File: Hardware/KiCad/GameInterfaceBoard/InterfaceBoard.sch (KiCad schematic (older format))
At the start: 34 parts, among them J1 CONN_11LOCK, J2 CONN_07LOCK

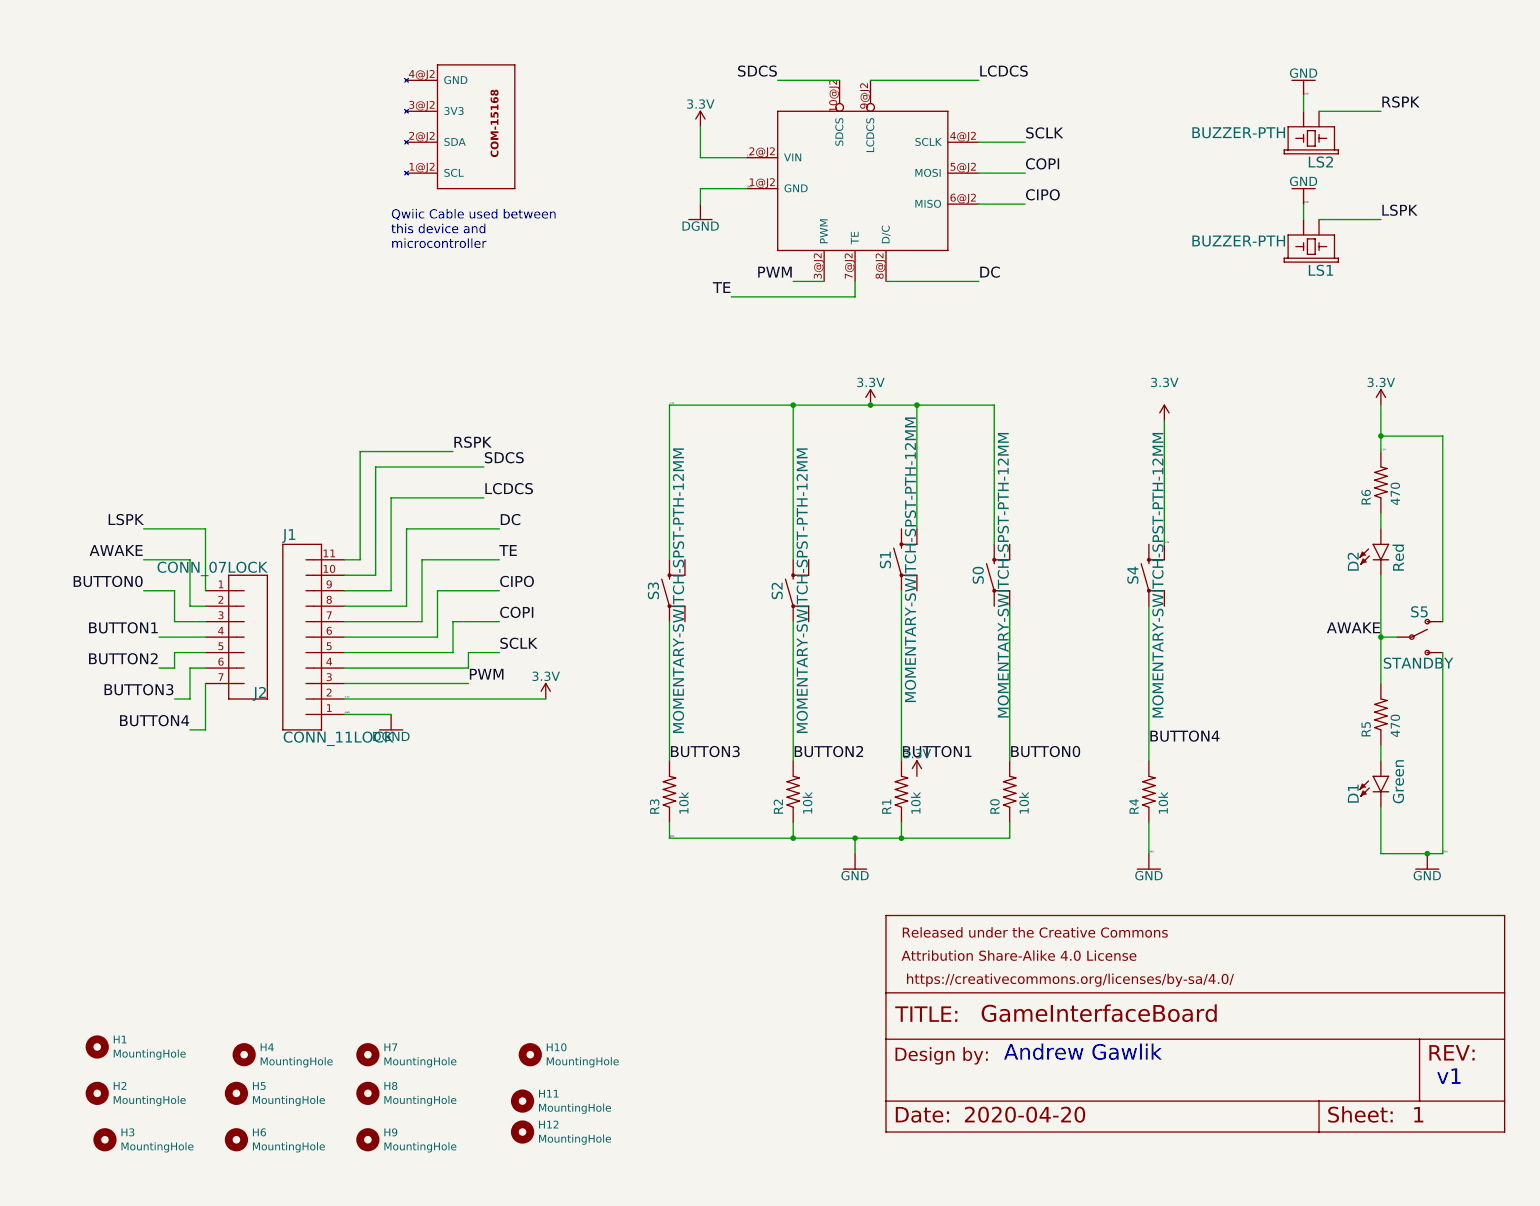
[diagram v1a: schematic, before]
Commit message: Removed excess drill holes as requested on issue #17
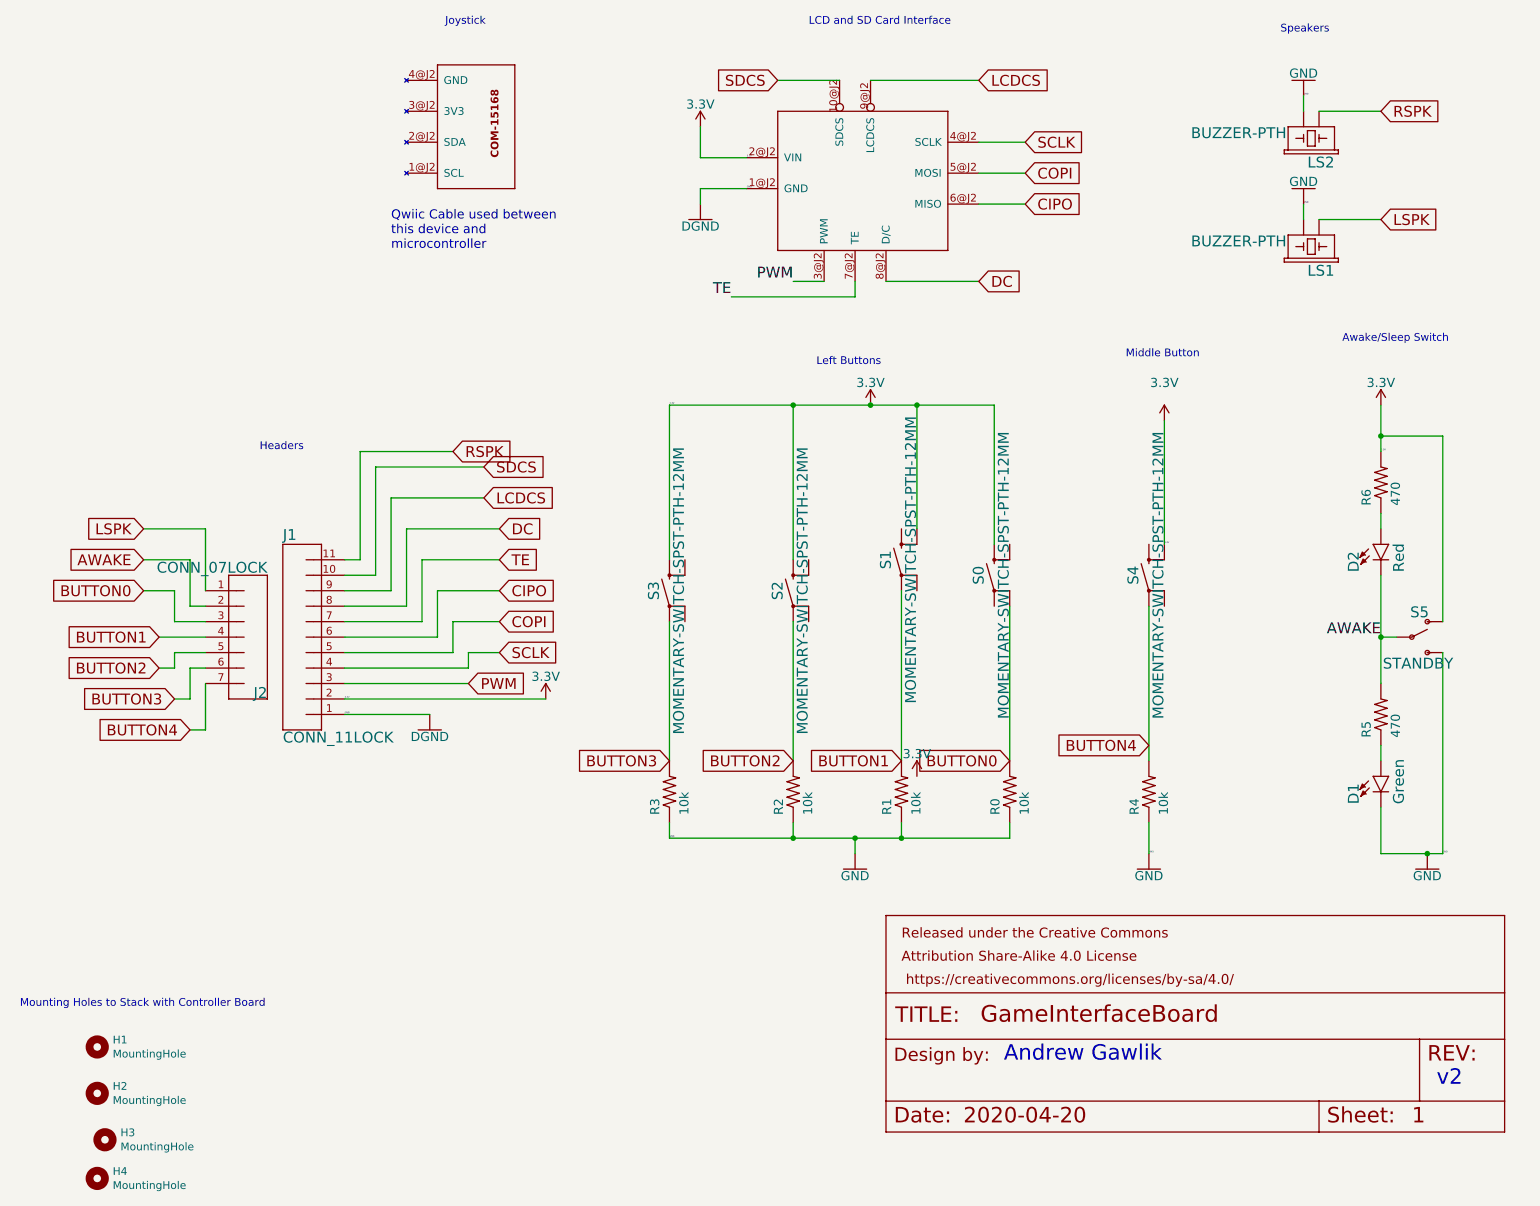
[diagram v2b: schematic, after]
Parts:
- removed H10, H11, H12, H5, H6, H7, H8, H9: MountingHole, MountingHole_3mm, symbol Mechanical:MountingHole
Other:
- note added: "Awake/Sleep Switch"
- note added: "Headers"
- note added: "Joystick"
- note added: "LCD and SD Card Interface"
- note added: "Left Buttons"
- note added: "Middle Button"
- note added: "Mounting Holes to Stack with Controller Board"
- note added: "Speakers"
- note added: "v2"
- note removed: "v1"
- moved on the sheet: H4
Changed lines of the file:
@@
 Wire Wire Line
 	5500 5600 5500 4700
-Text Label 5500 5600 0    70   ~ 0
-BUTTON3
 Wire Wire Line
 	2500 5000 2400 5000
@@
 Wire Wire Line
 	2400 5200 2300 5200
-Text Label 2300 5200 2    70   ~ 0
-BUTTON3
 Wire Wire Line
 	7700 4600 7700 5600
-Text Label 7700 5600 0    70   ~ 0
-BUTTON0
 Wire Wire Line
 	2500 4700 2300 4700
@@
 Wire Wire Line
 	2300 4500 2100 4500
-Text Label 2100 4500 2    70   ~ 0
-BUTTON0
 Wire Wire Line
 	6300 5600 6300 4700
-Text Label 6300 5600 0    70   ~ 0
-BUTTON2
 Wire Wire Line
 	2500 4900 2300 4900
@@
 Wire Wire Line
 	2300 5000 2200 5000
-Text Label 2200 5000 2    70   ~ 0
-BUTTON2
 Wire Wire Line
 	7000 4500 7000 5600
-Text Label 7000 5600 0    70   ~ 0
-BUTTON1
 Wire Wire Line
 	2500 4800 2200 4800
-Text Label 2200 4800 2    70   ~ 0
-BUTTON1
 Wire Wire Line
 	8600 6200 8600 6000
@@
 Text Label 6000 1900 0    10   ~ 0
 GND
-Wire Wire Line
-	3400 5300 3700 5300
 Text Label 3400 5300 0    10   ~ 0
 GND
@@
 Wire Wire Line
 	8600 4600 8600 5600
-Text Label 8600 5500 0    70   ~ 0
-BUTTON4
 Wire Wire Line
 	2500 5100 2500 5400
 Wire Wire Line
 	2500 5400 2400 5400
-Text Label 2400 5400 2    70   ~ 0
-BUTTON4
 Wire Wire Line
 	10100 5600 10100 5500
@@
 Wire Wire Line
 	2400 4300 2100 4300
-Text Label 2100 4300 2    70   ~ 0
-AWAKE
 Wire Wire Line
 	10100 4100 10100 4000
 Wire Wire Line
 	9700 2100 10100 2100
-Text Label 10100 2100 0    70   ~ 0
-LSPK
 Wire Wire Line
 	2500 4500 2500 4100
 Wire Wire Line
 	2500 4100 2100 4100
-Text Label 2100 4100 2    70   ~ 0
-LSPK
 Wire Wire Line
 	6500 2500 6300 2500
@@
 Wire Wire Line
 	3400 5100 4200 5100
-Text Label 4200 5100 0    70   ~ 0
-PWM
 Wire Wire Line
 	6700 2500 6700 2600
@@
 Wire Wire Line
 	3900 4300 4400 4300
-Text Label 4400 4300 0    70   ~ 0
-TE
 Wire Wire Line
 	6900 2500 7500 2500
-Text Label 7500 2500 0    70   ~ 0
-DC
 Wire Wire Line
 	3400 4600 3800 4600
@@
 Wire Wire Line
 	3800 4100 4400 4100
-Text Label 4400 4100 0    70   ~ 0
-DC
 Wire Wire Line
 	7500 2000 7800 2000
-Text Label 7800 2000 0    70   ~ 0
-CIPO
 Wire Wire Line
 	4000 4500 4400 4500
@@
 Wire Wire Line
 	4000 4800 4000 4500
-Text Label 4400 4500 0    70   ~ 0
-CIPO
 Wire Wire Line
 	7500 1800 7800 1800
-Text Label 7800 1800 0    70   ~ 0
-COPI
 Wire Wire Line
 	3400 4900 4100 4900
@@
 Wire Wire Line
 	4100 4700 4400 4700
-Text Label 4400 4700 0    70   ~ 0
-COPI
 Wire Wire Line
 	7500 1600 7800 1600
-Text Label 7800 1600 0    70   ~ 0
-SCLK
 Wire Wire Line
 	3400 5000 4200 5000
@@
 Wire Wire Line
 	4200 4900 4400 4900
-Text Label 4400 4900 0    70   ~ 0
-SCLK
 Wire Wire Line
 	6800 1200 7500 1200
-Text Label 7500 1200 0    70   ~ 0
-LCDCS
 Wire Wire Line
 	3400 4500 3700 4500
@@
 Wire Wire Line
 	3700 3900 4300 3900
-Text Label 4300 3900 0    70   ~ 0
-LCDCS
 Wire Wire Line
 	6600 1200 6200 1200
-Text Label 6200 1200 2    70   ~ 0
-SDCS
 Wire Wire Line
 	3400 4400 3600 4400
@@
 Wire Wire Line
 	3600 3700 4300 3700
-Text Label 4300 3700 0    70   ~ 0
-SDCS
 Wire Wire Line
 	9700 1400 10100 1400
-Text Label 10100 1400 0    70   ~ 0
-RSPK
 Wire Wire Line
 	3400 4300 3500 4300
@@
 Wire Wire Line
 	3500 3600 4100 3600
-Text Label 4100 3600 0    70   ~ 0
-RSPK
 $Comp
 L InterfaceBoard-eagle-import:R-US_0204_5 R2
@@
 $EndComp
 $Comp
-L InterfaceBoard-eagle-import:DGND #GND02
-U 1 1 13A376EC
-P 3700 5400
-F 0 "#GND02" H 3700 5400 50  0001 C CNN
-F 1 "DGND" H 3700 5390 59  0000 C TNN
-F 2 "" H 3700 5400 50  0001 C CNN
-F 3 "" H 3700 5400 50  0001 C CNN
-	1    3700 5400
-	1    0    0    -1
-$EndComp
-$Comp
 L InterfaceBoard-eagle-import:CONN_11LOCK J1
 U 1 1 2CE6A523
@@
 Andrew Gawlik
 Text Notes 10460 7710 0    100  ~ 0
-v1
+v2
 Text Notes 3700 2300 0    59   ~ 0
 Qwiic Cable used between\nthis device and\nmicrocontroller
@@
 L Mechanical:MountingHole H4
 U 1 1 60808813
-P 2750 7500
-F 0 "H4" H 2850 7546 50  0000 L CNN
-F 1 "MountingHole" H 2850 7455 50  0000 L CNN
-F 2 "MountingHole_3mm" H 2750 7500 50  0001 C CNN
-F 3 "~" H 2750 7500 50  0001 C CNN
-	1    2750 7500
+P 1800 8300
+F 0 "H4" H 1900 8346 50  0000 L CNN
+F 1 "MountingHole" H 1900 8255 50  0000 L CNN
+F 2 "MountingHole_3mm" H 1800 8300 50  0001 C CNN
+F 3 "~" H 1800 8300 50  0001 C CNN
+	1    1800 8300
 	1    0    0    -1
 $EndComp
@@
 $EndComp
 $Comp
-L Mechanical:MountingHole H7
-U 1 1 6081064F
-P 3550 7500
-F 0 "H7" H 3650 7546 50  0000 L CNN
-F 1 "MountingHole" H 3650 7455 50  0000 L CNN
-F 2 "MountingHole_3mm" H 3550 7500 50  0001 C CNN
-F 3 "~" H 3550 7500 50  0001 C CNN
-	1    3550 7500
-	1    0    0    -1
-$EndComp
-$Comp
-L Mechanical:MountingHole H8
-U 1 1 60810B66
-P 3550 7750
-F 0 "H8" H 3650 7796 50  0000 L CNN
-F 1 "MountingHole" H 3650 7705 50  0000 L CNN
-F 2 "MountingHole_3mm" H 3550 7750 50  0001 C CNN
-F 3 "~" H 3550 7750 50  0001 C CNN
-	1    3550 7750
-	1    0    0    -1
-$EndComp
-$Comp
 L Mechanical:MountingHole H3
 U 1 1 608113E1
@@
 $EndComp
 $Comp
-L Mechanical:MountingHole H6
-U 1 1 60811785
-P 2700 8050
-F 0 "H6" H 2800 8096 50  0000 L CNN
-F 1 "MountingHole" H 2800 8005 50  0000 L CNN
-F 2 "MountingHole_3mm" H 2700 8050 50  0001 C CNN
-F 3 "~" H 2700 8050 50  0001 C CNN
-	1    2700 8050
-	1    0    0    -1
-$EndComp
-$Comp
-L Mechanical:MountingHole H10
-U 1 1 60811E6B
-P 4600 7500
-F 0 "H10" H 4700 7546 50  0000 L CNN
-F 1 "MountingHole" H 4700 7455 50  0000 L CNN
-F 2 "MountingHole_3mm" H 4600 7500 50  0001 C CNN
-F 3 "~" H 4600 7500 50  0001 C CNN
-	1    4600 7500
-	1    0    0    -1
-$EndComp
-$Comp
-L Mechanical:MountingHole H12
-U 1 1 6081248E
-P 4550 8000
-F 0 "H12" H 4650 8046 50  0000 L CNN
-F 1 "MountingHole" H 4650 7955 50  0000 L CNN
-F 2 "MountingHole_3mm" H 4550 8000 50  0001 C CNN
-F 3 "~" H 4550 8000 50  0001 C CNN
-	1    4550 8000
-	1    0    0    -1
-$EndComp
-$Comp
 L Mechanical:MountingHole H2
 U 1 1 60812A9E
@@
 	1    0    0    -1
 $EndComp
+Text GLabel 2100 4100 0    70   Input ~ 0
+LSPK
+Text GLabel 2100 4300 0    70   Input ~ 0
+AWAKE
+Text GLabel 2100 4500 0    70   Input ~ 0
+BUTTON0
+Text GLabel 2200 4800 0    70   Input ~ 0
+BUTTON1
+Text GLabel 2200 5000 0    70   Input ~ 0
+BUTTON2
+Text GLabel 2300 5200 0    70   Input ~ 0
+BUTTON3
+Text GLabel 2400 5400 0    70   Input ~ 0
+BUTTON4
+Text GLabel 4100 3600 2    70   Input ~ 0
+RSPK
+Text GLabel 4300 3700 2    70   Input ~ 0
+SDCS
+Text GLabel 4300 3900 2    70   Input ~ 0
+LCDCS
+Text GLabel 4400 4100 2    70   Input ~ 0
+DC
+Text GLabel 4400 4300 2    70   Input ~ 0
+TE
+Text GLabel 4400 4500 2    70   Input ~ 0
+CIPO
+Text GLabel 4400 4700 2    70   Input ~ 0
+COPI
+Text GLabel 4400 4900 2    70   Input ~ 0
+SCLK
+Text GLabel 4200 5100 2    70   Input ~ 0
+PWM
 $Comp
-L Mechanical:MountingHole H5
-U 1 1 60813FB8
-P 2700 7750
-F 0 "H5" H 2800 7796 50  0000 L CNN
-F 1 "MountingHole" H 2800 7705 50  0000 L CNN
-F 2 "MountingHole_3mm" H 2700 7750 50  0001 C CNN
-F 3 "~" H 2700 7750 50  0001 C CNN
-	1    2700 7750
-	1    0    0    -1
-$EndComp
-$Comp
-L Mechanical:MountingHole H9
-U 1 1 60814652
-P 3550 8050
-F 0 "H9" H 3650 8096 50  0000 L CNN
-F 1 "MountingHole" H 3650 8005 50  0000 L CNN
-F 2 "MountingHole_3mm" H 3550 8050 50  0001 C CNN
-F 3 "~" H 3550 8050 50  0001 C CNN
-	1    3550 8050
-	1    0    0    -1
-$EndComp
-$Comp
-L Mechanical:MountingHole H11
-U 1 1 60814DD4
-P 4550 7800
-F 0 "H11" H 4650 7846 50  0000 L CNN
-F 1 "MountingHole" H 4650 7755 50  0000 L CNN
-F 2 "MountingHole_3mm" H 4550 7800 50  0001 C CNN
-F 3 "~" H 4550 7800 50  0001 C CNN
-	1    4550 7800
+L InterfaceBoard-eagle-import:DGND #GND02
+U 1 1 13A376EC
+P 3950 5400
+F 0 "#GND02" H 3950 5400 50  0001 C CNN
+F 1 "DGND" H 3950 5390 59  0000 C TNN
+F 2 "" H 3950 5400 50  0001 C CNN
+F 3 "" H 3950 5400 50  0001 C CNN
+	1    3950 5400
 	1    0    0    -1
 $EndComp
+Wire Wire Line
+	3400 5300 3950 5300
+Text GLabel 5500 5600 0    70   Input ~ 0
+BUTTON3
+Text GLabel 6300 5600 0    70   Input ~ 0
+BUTTON2
+Text GLabel 7000 5600 0    70   Input ~ 0
+BUTTON1
+Text GLabel 7700 5600 0    70   Input ~ 0
+BUTTON0
+Text GLabel 8600 5500 0    70   Input ~ 0
+BUTTON4
+Text GLabel 7800 1600 2    70   Input ~ 0
+SCLK
+Text GLabel 7800 1800 2    70   Input ~ 0
+COPI
+Text GLabel 7800 2000 2    70   Input ~ 0
+CIPO
+Text GLabel 7500 2500 2    70   Input ~ 0
+DC
+Text GLabel 10100 1400 2    70   Input ~ 0
+RSPK
+Text GLabel 10100 2100 2    70   Input ~ 0
+LSPK
+Text GLabel 7500 1200 2    70   Input ~ 0
+LCDCS
+Text GLabel 6200 1200 0    70   Input ~ 0
+SDCS
+Text Notes 2850 3600 0    50   ~ 0
+Headers
+Text Notes 6450 3050 0    50   ~ 0
+Left Buttons
+Text Notes 8450 3000 0    50   ~ 0
+Middle Button
+Text Notes 9850 2900 0    50   ~ 0
+Awake/Sleep Switch
+Text Notes 9450 900  0    50   ~ 0
+Speakers
+Text Notes 6400 850  0    50   ~ 0
+LCD and SD Card Interface
+Text Notes 4050 850  0    50   ~ 0
+Joystick
+Text Notes 1300 7200 0    50   ~ 0
+Mounting Holes to Stack with Controller Board
 $EndSCHEMATC
